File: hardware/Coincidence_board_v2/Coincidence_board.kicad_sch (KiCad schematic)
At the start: 70 parts, among them J1 Inputs, J2 chan2_in, J3 POWER_IN, J4 Morpho_Gauche, J5 chan3_out, J7 Morpho_Droite, SW1 SW_1, U1 74HCT74, U2 74HCT74, U3 LM7805_TO220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

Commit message: Update Coincidence Board / v2
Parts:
- removed D2, D3, D4, D5, D6, D7: 1N4148, Diode_THT:D_DO-35_SOD27_P7.62mm_Horizontal, symbol Diode:1N4148
- removed J4: Morpho_Gauche, Connector_PinHeader_2.54mm:PinHeader_2x20_P2.54mm_Vertical, symbol Connector_Generic:Conn_02x20_Odd_Even
- removed J7: Morpho_Droite, Connector_PinHeader_2.54mm:PinHeader_2x20_P2.54mm_Vertical, symbol Connector_Generic:Conn_02x20_Odd_Even
- added U8: NUCLEO-L432KC, NUCLEO_L432KC:MODULE_NUCLEO-L432KC, symbol NUCLEO-L432KC:NUCLEO-L432KC
- U1, U2, U4, U5, U6, U7: footprint Package_SO:SO-14_3.9x8.65mm_P1.27mm -> Package_DIP:DIP-14_W7.62mm_Socket_LongPads
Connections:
- net 3.3V_NUC: now also U8.CN4_14 (+3V3)
- net 5V_NUC: now also U8.CN4_4 (+5V)
- net A2out_nuc: now also U8.CN4_11 (PA1)
- net AB2out_nuc: now also U8.CN3_12 (PA8)
- net ABCout_nuc: now also U8.CN3_1 (PA9)
- net AC2out_nuc: now also U8.CN3_14 (PB5)
- net B2out_nuc: now also U8.CN4_9 (PA4)
- net BC2out_nuc: now also U8.CN3_5 (PA12)
- net C2out_nuc: now also U8.CN4_7 (PA6)
- net GND: now also U8.CN3_4 (GND_CN3), U8.CN4_2 (GND_CN4)
- net LED_OUT: now also U8.CN3_6 (PB0)
- net POT_OUT: now also U8.CN4_5 (PA2)
- net SW1_OUT: now also U8.CN3_7 (PB7)
- net VIN: now also U8.CN4_1 (VIN)
- no-connect marks 28 -> 0
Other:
- note removed: "PA_0"
- note removed: "PA_1"
- note removed: "PA_11"
- note removed: "PA_12"
- note removed: "PA_13"
- note removed: "PA_14"
- note removed: "PA_15"
- note removed: "PA_4"
- note removed: "PA_5"
- note removed: "PA_6"
- note removed: "PA_7"
- note removed: "PB_0"
- note removed: "PB_1"
- note removed: "PB_11"
- note removed: "PB_12"
- note removed: "PB_13"
- note removed: "PB_14"
- note removed: "PB_2"
- note removed: "PB_3"
- note removed: "PB_4"
- note removed: "PB_5"
- note removed: "PB_7"
- note removed: "PB_8"
- note removed: "PB_9"
- note removed: "PC_0"
- note removed: "PC_1"
- note removed: "PC_10"
- note removed: "PC_11"
- note removed: "PC_12"
- note removed: "PC_13"
- note removed: "PC_2"
- note removed: "PC_3"
- note removed: "PC_4"
- note removed: "PC_5"
- note removed: "PC_6"
- note removed: "PC_7"
- note removed: "PC_8"
- note removed: "PD_2"

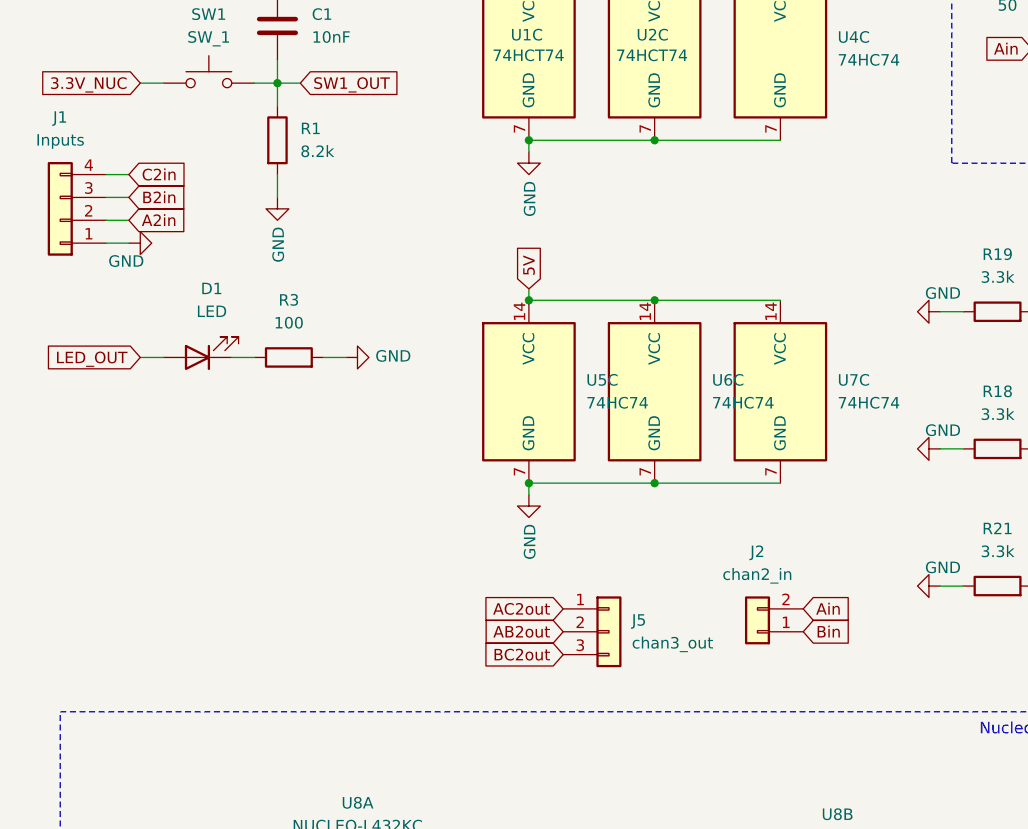
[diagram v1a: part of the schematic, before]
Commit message: Update GRA experiment / Creating new electronic interface based on G431KB Nucleo board
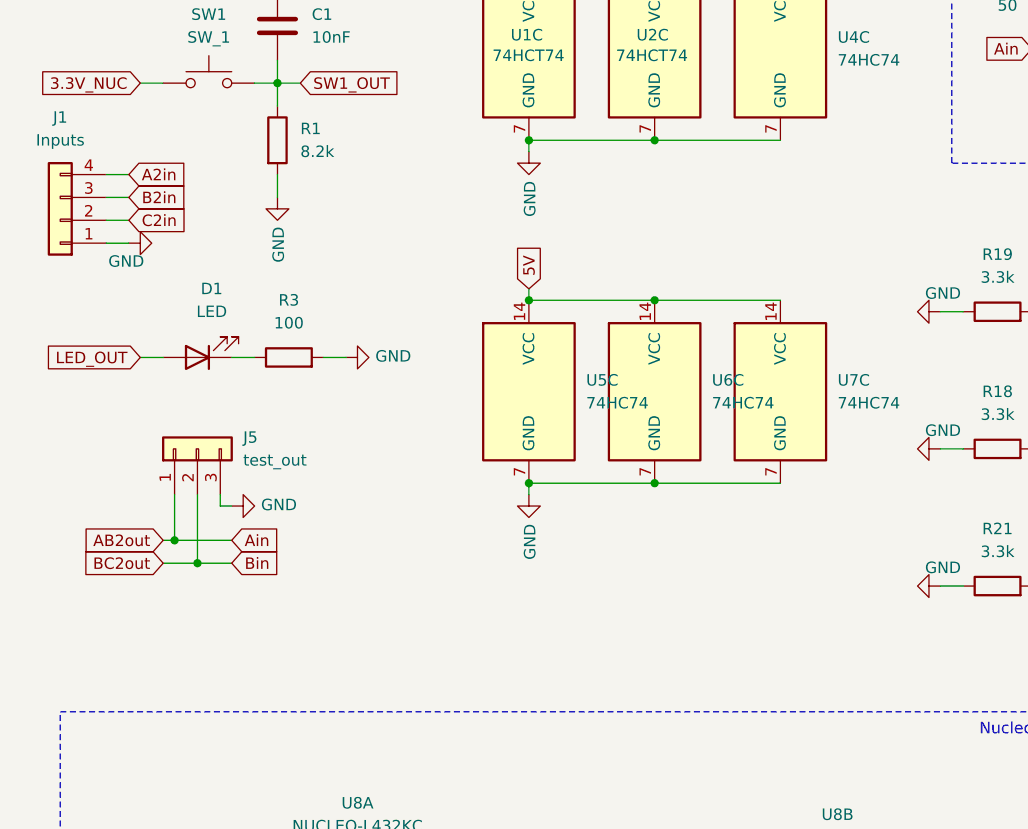
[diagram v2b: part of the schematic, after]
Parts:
- removed J2: chan2_in, Connector_PinHeader_2.54mm:PinHeader_1x02_P2.54mm_Vertical, symbol Connector_Generic:Conn_01x02
- J5: value chan3_out -> test_out
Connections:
- net Ain is gone; now on net AB2out: R6.2, U1.12 (D), U2.11 (C)
- net Bin is gone; now on net BC2out: R5.1, U1.3 (C)
- net A2in: now also J1.4 (Pin_4); no longer J1.2 (Pin_2)
- net AB2out: now also J5.1 (Pin_1); no longer J5.2 (Pin_2)
- net AC2out: no longer J5.1 (Pin_1)
- net BC2out: now also J5.2 (Pin_2); no longer J5.3 (Pin_3)
- net C2in: now also J1.2 (Pin_2); no longer J1.4 (Pin_4)
- net GND: now also J5.3 (Pin_3)
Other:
- moved on the sheet: J5
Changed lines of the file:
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@@
 	)
 	(junction
+		(at 29.21 118.11)
+		(diameter 0)
+		(color 0 0 0 0)
+	)
+	(junction
 		(at 165.1 53.34)
 		(diameter 0)
@@
 	)
 	(junction
+		(at 31.75 120.65)
+		(diameter 0)
+		(color 0 0 0 0)
+	)
+	(junction
 		(at 71.12 21.59)
 		(diameter 0)
@@
 	(wire
 		(pts
+			(xy 27.94 118.11) (xy 29.21 118.11)
+		)
+		(stroke
+			(width 0)
+			(type default)
+		)
+	)
+	(wire
+		(pts
 			(xy 218.44 83.82) (xy 218.44 85.09)
 		)
@@
 	(wire
 		(pts
+			(xy 34.29 114.3) (xy 35.56 114.3)
+		)
+		(stroke
+			(width 0)
+			(type default)
+		)
+	)
+	(wire
+		(pts
 			(xy 255.27 48.26) (xy 255.27 46.99)
 		)
@@
 	(wire
 		(pts
+			(xy 27.94 120.65) (xy 31.75 120.65)
+		)
+		(stroke
+			(width 0)
+			(type default)
+		)
+	)
+	(wire
+		(pts
 			(xy 245.11 39.37) (xy 247.65 39.37)
 		)
@@
 	(wire
 		(pts
+			(xy 29.21 113.03) (xy 29.21 118.11)
+		)
+		(stroke
+			(width 0)
+			(type default)
+		)
+	)
+	(wire
+		(pts
 			(xy 166.37 138.43) (xy 168.91 138.43)
 		)
@@
 	(wire
 		(pts
+			(xy 31.75 120.65) (xy 35.56 120.65)
+		)
+		(stroke
+			(width 0)
+			(type default)
+		)
+	)
+	(wire
+		(pts
 			(xy 240.03 93.98) (xy 240.03 109.22)
 		)
@@
 		)
 	)
+	(wire
+		(pts
+			(xy 29.21 118.11) (xy 35.56 118.11)
+		)
+		(stroke
+			(width 0)
+			(type default)
+		)
+	)
 	(polyline
 		(pts
@@
 	(wire
 		(pts
+			(xy 34.29 113.03) (xy 34.29 114.3)
+		)
+		(stroke
+			(width 0)
+			(type default)
+		)
+	)
+	(wire
+		(pts
 			(xy 68.58 90.17) (xy 68.58 91.44)
 		)
@@
 	(wire
 		(pts
+			(xy 31.75 120.65) (xy 31.75 113.03)
+		)
+		(stroke
+			(width 0)
+			(type default)
+		)
+	)
+	(wire
+		(pts
 			(xy 48.26 20.32) (xy 48.26 21.59)
 		)
@@
 	(global_label "A2in"
 		(shape input)
-		(at 24.13 82.55 0)
+		(at 24.13 77.47 0)
 		(fields_autoplaced yes)
 		(effects
@@
 		)
 		(property "Intersheetrefs" "${INTERSHEET_REFS}"
-			(at 30.5129 82.55 0)
+			(at 30.5129 77.47 0)
 			(effects
 				(font
@@
 		)
 	)
+	(global_label "AB2out"
+		(shape input)
+		(at 27.94 118.11 180)
+		(fields_autoplaced yes)
+		(effects
+			(font
+				(size 1.27 1.27)
+			)
+			(justify right)
+		)
+		(property "Intersheetrefs" "${INTERSHEET_REFS}"
+			(at 19.0172 118.11 0)
+			(effects
+				(font
+					(size 1.27 1.27)
+				)
+				(justify right)
+				(hide yes)
+			)
+		)
+	)
 	(global_label "LED_OUT"
 		(shape input)
@@
 	(global_label "C2in"
 		(shape input)
-		(at 24.13 77.47 0)
+		(at 24.13 82.55 0)
 		(fields_autoplaced yes)
 		(effects
@@
 		)
 		(property "Intersheetrefs" "${INTERSHEET_REFS}"
-			(at 30.6943 77.47 0)
+			(at 30.6943 82.55 0)
 			(effects
 				(font
@@
 	(global_label "Ain"
 		(shape input)
-		(at 99.06 125.73 0)
+		(at 35.56 118.11 0)
 		(fields_autoplaced yes)
 		(effects
@@
 		)
 		(property "Intersheetrefs" "${INTERSHEET_REFS}"
-			(at 104.2334 125.73 0)
+			(at 40.7334 118.11 0)
 			(effects
 				(font
@@
 		)
 	)
-	(global_label "AB2out"
-		(shape input)
-		(at 72.39 128.27 180)
-		(fields_autoplaced yes)
-		(effects
-			(font
-				(size 1.27 1.27)
-			)
-			(justify right)
-		)
-		(property "Intersheetrefs" "${INTERSHEET_REFS}"
-			(at 63.4672 128.27 0)
-			(effects
-				(font
-					(size 1.27 1.27)
-				)
-				(justify right)
-				(hide yes)
-			)
-		)
-	)
 	(global_label "VIN"
 		(shape input)
@@
 	(global_label "Bin"
 		(shape input)
-		(at 99.06 128.27 0)
+		(at 35.56 120.65 0)
 		(fields_autoplaced yes)
 		(effects
@@
 		)
 		(property "Intersheetrefs" "${INTERSHEET_REFS}"
-			(at 104.4148 128.27 0)
+			(at 40.9148 120.65 0)
 			(effects
 				(font
@@
 	(global_label "BC2out"
 		(shape input)
-		(at 72.39 130.81 180)
+		(at 27.94 120.65 180)
 		(fields_autoplaced yes)
 		(effects
@@
 		)
 		(property "Intersheetrefs" "${INTERSHEET_REFS}"
-			(at 63.2858 130.81 0)
+			(at 18.8358 120.65 0)
 			(effects
 				(font
@@
 		)
 	)
-	(global_label "AC2out"
-		(shape input)
-		(at 72.39 125.73 180)
-		(fields_autoplaced yes)
-		(effects
-			(font
-				(size 1.27 1.27)
-			)
-			(justify right)
-		)
-		(property "Intersheetrefs" "${INTERSHEET_REFS}"
-			(at 63.4672 125.73 0)
-			(effects
-				(font
-					(size 1.27 1.27)
-				)
-				(justify right)
-				(hide yes)
-			)
-		)
-	)
 	(global_label "5V"
 		(shape input)
@@
 	)
 	(symbol
+		(lib_id "power:GND")
+		(at 35.56 114.3 90)
+		(unit 1)
+		(exclude_from_sim no)
+		(in_bom yes)
+		(on_board yes)
+		(dnp no)
+		(property "Reference" "#PWR012"
+			(at 41.91 114.3 0)
+			(effects
+				(font
+					(size 1.27 1.27)
+				)
+				(hide yes)
+			)
+		)
+		(property "Value" "GND"
+			(at 38.8112 114.173 90)
+			(effects
+				(font
+					(size 1.27 1.27)
+				)
+				(justify right)
+			)
+		)
+		(property "Footprint" ""
+			(at 35.56 114.3 0)
+			(effects
+				(font
+					(size 1.27 1.27)
+				)
+				(hide yes)
+			)
+		)
+		(property "Datasheet" ""
+			(at 35.56 114.3 0)
+			(effects
+				(font
+					(size 1.27 1.27)
+				)
+				(hide yes)
+			)
+		)
+		(property "Description" ""
+			(at 35.56 114.3 0)
+			(effects
+				(font
+					(size 1.27 1.27)
+				)
+				(hide yes)
+			)
+		)
+		(pin "1"
+		)
+		(instances
+			(project "Coincidence_board"
+				(path "/44ad8000-4ee7-4966-8fe6-195894dfb602"
+					(reference "#PWR012")
+					(unit 1)
+				)
+			)
+		)
+	)
+	(symbol
 		(lib_id "74xx:74HC74")
 		(at 68.58 101.6 0)
@@
 	)
 	(symbol
-		(lib_id "Connector_Generic:Conn_01x02")
-		(at 93.98 128.27 180)
-		(unit 1)
-		(exclude_from_sim no)
-		(in_bom yes)
-		(on_board yes)
-		(dnp no)
-		(fields_autoplaced yes)
-		(property "Reference" "J2"
-			(at 93.98 119.38 0)
-			(effects
-				(font
-					(size 1.27 1.27)
-				)
-			)
-		)
-		(property "Value" "chan2_in"
-			(at 93.98 121.92 0)
-			(effects
-				(font
-					(size 1.27 1.27)
-				)
-			)
-		)
-		(property "Footprint" "Connector_PinHeader_2.54mm:PinHeader_1x02_P2.54mm_Vertical"
-			(at 93.98 128.27 0)
-			(effects
-				(font
-					(size 1.27 1.27)
-				)
-				(hide yes)
-			)
-		)
-		(property "Datasheet" "~"
-			(at 93.98 128.27 0)
-			(effects
-				(font
-					(size 1.27 1.27)
-				)
-				(hide yes)
-			)
-		)
-		(property "Description" "Generic connector, single row, 01x02, script generated (kicad-library-utils/schlib/autogen/connector/)"
-			(at 93.98 128.27 0)
-			(effects
-				(font
-					(size 1.27 1.27)
-				)
-				(hide yes)
-			)
-		)
-		(pin "1"
-		)
-		(pin "2"
-		)
-		(instances
-			(project "Coincidence_board"
-				(path "/44ad8000-4ee7-4966-8fe6-195894dfb602"
-					(reference "J2")
-					(unit 1)
-				)
-			)
-		)
-	)
-	(symbol
 		(lib_id "Device:C")
 		(at 71.12 36.83 0)
@@
 	(symbol
 		(lib_id "Connector_Generic:Conn_01x03")
-		(at 77.47 128.27 0)
+		(at 31.75 107.95 90)
 		(unit 1)
 		(exclude_from_sim no)
@@
 		(fields_autoplaced yes)
 		(property "Reference" "J5"
-			(at 80.01 126.9999 0)
+			(at 36.83 106.6799 90)
 			(effects
 				(font
 					(size 1.27 1.27)
 				)
-				(justify left)
+				(justify right)
 			)
 		)
-		(property "Value" "chan3_out"
-			(at 80.01 129.5399 0)
+		(property "Value" "test_out"
+			(at 36.83 109.2199 90)
 			(effects
 				(font
 					(size 1.27 1.27)
 				)
-				(justify left)
+				(justify right)
 			)
 		)
 		(property "Footprint" "Connector_PinHeader_2.54mm:PinHeader_1x03_P2.54mm_Vertical"
-			(at 77.47 128.27 0)
+			(at 31.75 107.95 0)
 			(effects
 				(font
@@
 		)
 		(property "Datasheet" "~"
-			(at 77.47 128.27 0)
+			(at 31.75 107.95 0)
 			(effects
 				(font
@@
 		)
 		(property "Description" "Generic connector, single row, 01x03, script generated (kicad-library-utils/schlib/autogen/connector/)"
-			(at 77.47 128.27 0)
+			(at 31.75 107.95 0)
 			(effects
 				(font
